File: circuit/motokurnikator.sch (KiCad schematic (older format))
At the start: 13 parts, among them IC1 ATTINY84-P, P1 MOTOR, SW1 END_SW, SW2 END_SW, SW3 MANUAL_OPEN, U1 LM7805CT

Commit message: Add a missing resistor.
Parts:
- added R4: 1k, symbol R
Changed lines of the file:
@@
 L GND #PWR9
 U 1 1 553CC16E
-P 5500 3750
-F 0 "#PWR9" H 5500 3750 30  0001 C CNN
-F 1 "GND" H 5500 3680 30  0001 C CNN
-F 2 "" H 5500 3750 60  0000 C CNN
-F 3 "" H 5500 3750 60  0000 C CNN
-	1    5500 3750
+P 6000 3750
+F 0 "#PWR9" H 6000 3750 30  0001 C CNN
+F 1 "GND" H 6000 3680 30  0001 C CNN
+F 2 "" H 6000 3750 60  0000 C CNN
+F 3 "" H 6000 3750 60  0000 C CNN
+	1    6000 3750
 	0    -1   -1   0
 $EndComp
@@
 Text Notes 10600 7650 0    60   ~ 0
 2
+$Comp
+L R R4
+U 1 1 553D0A76
+P 5750 3750
+F 0 "R4" V 5830 3750 40  0000 C CNN
+F 1 "1k" V 5757 3751 40  0000 C CNN
+F 2 "" V 5680 3750 30  0000 C CNN
+F 3 "" H 5750 3750 30  0000 C CNN
+	1    5750 3750
+	0    1    1    0
+$EndComp
 $EndSCHEMATC

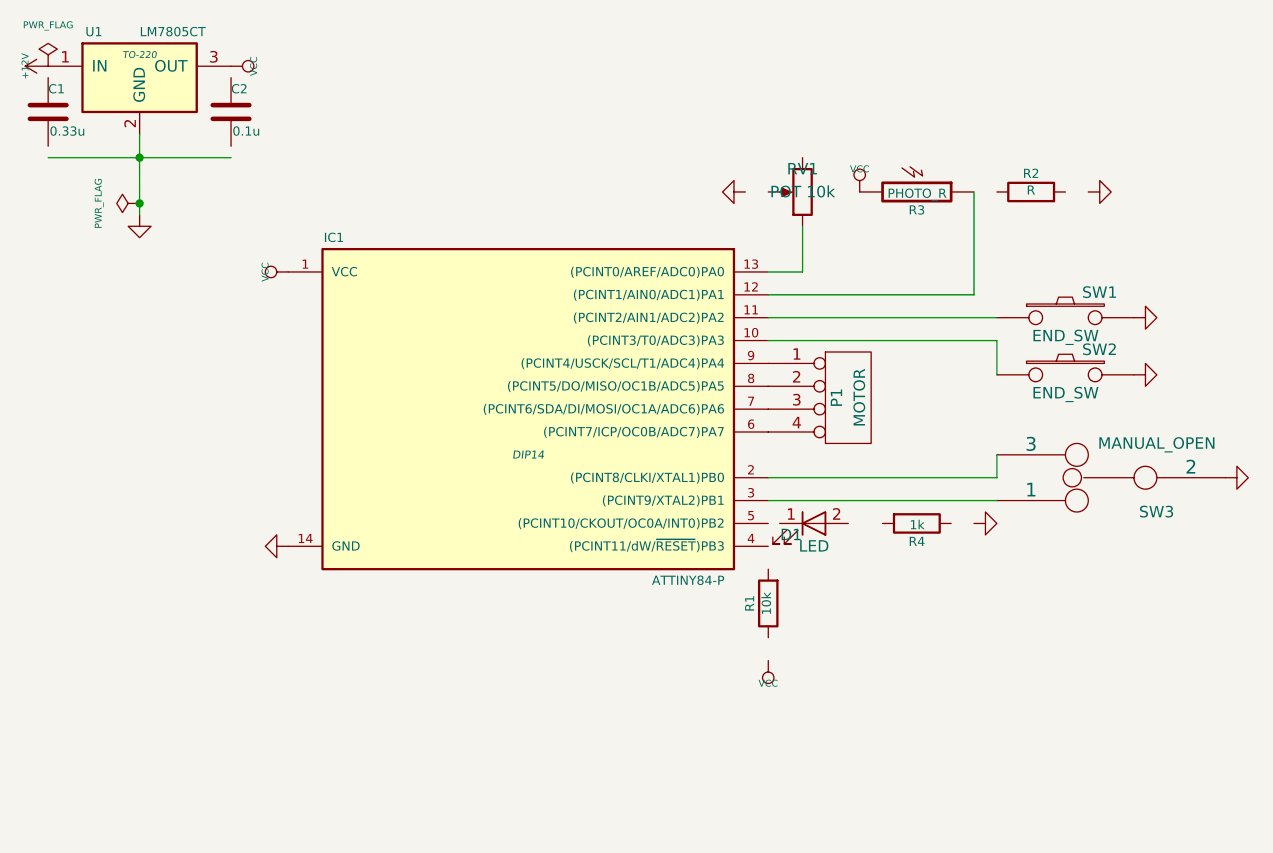
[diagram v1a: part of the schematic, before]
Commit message: Update schematic for newer symbol library.
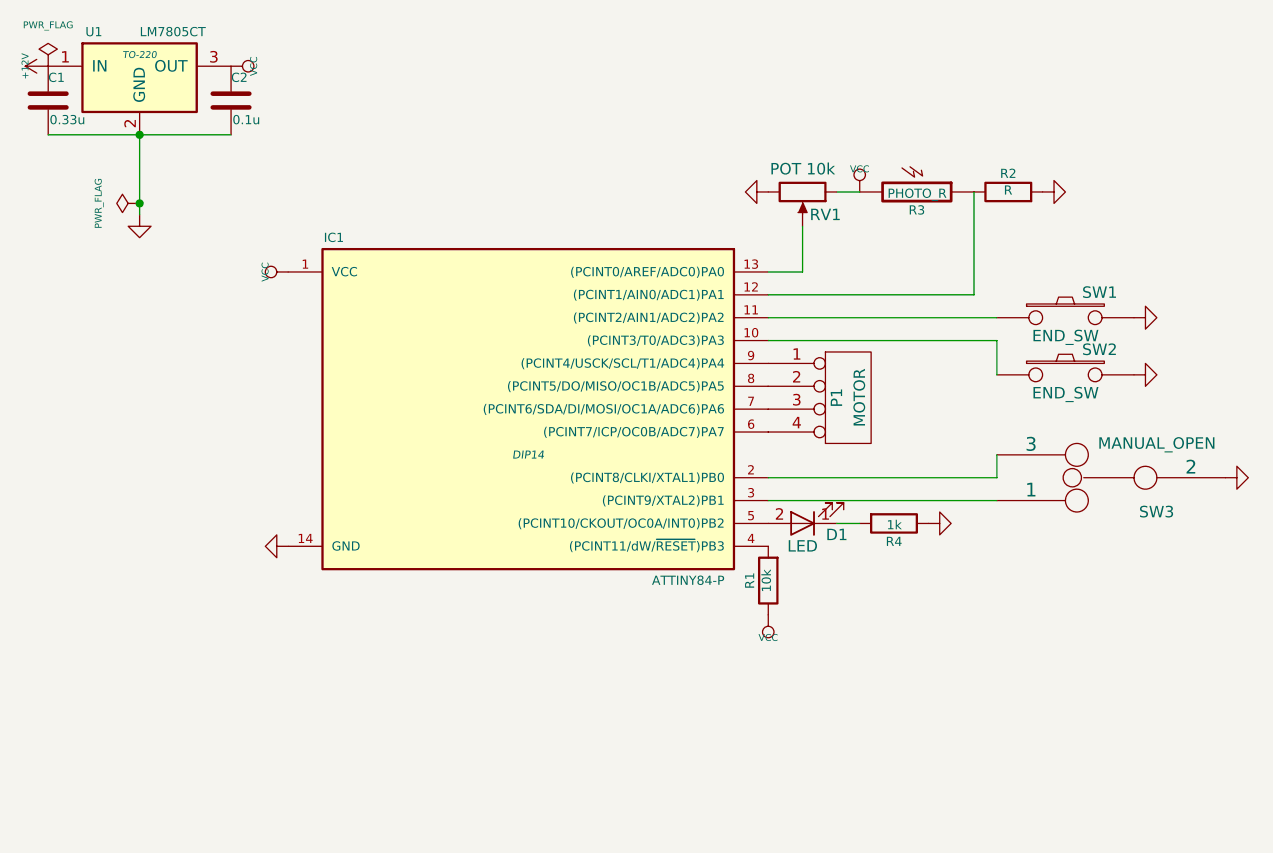
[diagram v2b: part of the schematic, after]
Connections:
- wire segments 12 -> 14
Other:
- moved on the sheet: C1, C2, D1, R1, R2, R4, RV1
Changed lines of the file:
@@
 LIBS:memory
 LIBS:xilinx
-LIBS:special
 LIBS:microcontrollers
 LIBS:dsp
@@
 U 1 1 55212F35
 P 5250 2300
-F 0 "RV1" H 5250 2200 50  0000 C CNN
-F 1 "POT 10k" H 5250 2300 50  0000 C CNN
+F 0 "RV1" V 5350 2400 50  0000 C CNN
+F 1 "POT 10k" V 5150 2300 50  0000 C CNN
 F 2 "" H 5250 2300 60  0000 C CNN
 F 3 "" H 5250 2300 60  0000 C CNN
 	1    5250 2300
-	-1   0    0    1
+	0    1    1    0
 $EndComp
 $Comp
 L GND #PWR6
 U 1 1 55212F76
-P 5000 2300
-F 0 "#PWR6" H 5000 2300 30  0001 C CNN
-F 1 "GND" H 5000 2230 30  0001 C CNN
-F 2 "" H 5000 2300 60  0000 C CNN
-F 3 "" H 5000 2300 60  0000 C CNN
-	1    5000 2300
+P 5100 2300
+F 0 "#PWR6" H 5100 2300 30  0001 C CNN
+F 1 "GND" H 5100 2230 30  0001 C CNN
+F 2 "" H 5100 2300 60  0000 C CNN
+F 3 "" H 5100 2300 60  0000 C CNN
+	1    5100 2300
 	0    1    1    0
 $EndComp
@@
 L R R2
 U 1 1 55212FCB
-P 6250 2300
-F 0 "R2" V 6330 2300 40  0000 C CNN
-F 1 "R" V 6257 2301 40  0000 C CNN
-F 2 "" V 6180 2300 30  0000 C CNN
-F 3 "" H 6250 2300 30  0000 C CNN
-	1    6250 2300
+P 6150 2300
+F 0 "R2" V 6230 2300 40  0000 C CNN
+F 1 "R" V 6157 2301 40  0000 C CNN
+F 2 "" V 6080 2300 30  0000 C CNN
+F 3 "" H 6150 2300 30  0000 C CNN
+	1    6150 2300
 	0    -1   -1   0
 $EndComp
@@
 L GND #PWR10
 U 1 1 55213508
-P 6500 2300
-F 0 "#PWR10" H 6500 2300 30  0001 C CNN
-F 1 "GND" H 6500 2230 30  0001 C CNN
-F 2 "" H 6500 2300 60  0000 C CNN
-F 3 "" H 6500 2300 60  0000 C CNN
-	1    6500 2300
+P 6300 2300
+F 0 "#PWR10" H 6300 2300 30  0001 C CNN
+F 1 "GND" H 6300 2230 30  0001 C CNN
+F 2 "" H 6300 2300 60  0000 C CNN
+F 3 "" H 6300 2300 60  0000 C CNN
+	1    6300 2300
 	0    -1   -1   0
 $EndComp
@@
 L R R1
 U 1 1 5521358D
-P 5100 4100
-F 0 "R1" V 5180 4100 40  0000 C CNN
-F 1 "10k" V 5107 4101 40  0000 C CNN
-F 2 "" V 5030 4100 30  0000 C CNN
-F 3 "" H 5100 4100 30  0000 C CNN
-	1    5100 4100
+P 5100 4000
+F 0 "R1" V 5180 4000 40  0000 C CNN
+F 1 "10k" V 5107 4001 40  0000 C CNN
+F 2 "" V 5030 4000 30  0000 C CNN
+F 3 "" H 5100 4000 30  0000 C CNN
+	1    5100 4000
 	-1   0    0    1
 $EndComp
@@
 L VCC #PWR7
 U 1 1 552135C4
-P 5100 4350
-F 0 "#PWR7" H 5100 4450 30  0001 C CNN
-F 1 "VCC" H 5100 4450 30  0000 C CNN
-F 2 "" H 5100 4350 60  0000 C CNN
-F 3 "" H 5100 4350 60  0000 C CNN
-	1    5100 4350
+P 5100 4150
+F 0 "#PWR7" H 5100 4250 30  0001 C CNN
+F 1 "VCC" H 5100 4250 30  0000 C CNN
+F 2 "" H 5100 4150 60  0000 C CNN
+F 3 "" H 5100 4150 60  0000 C CNN
+	1    5100 4150
 	-1   0    0    1
 $EndComp
@@
 L LED D1
 U 1 1 553CC120
-P 5300 3750
-F 0 "D1" H 5200 3700 50  0000 C CNN
-F 1 "LED" H 5300 3650 50  0000 C CNN
-F 2 "" H 5300 3750 60  0000 C CNN
-F 3 "" H 5300 3750 60  0000 C CNN
-	1    5300 3750
-	1    0    0    -1
+P 5250 3750
+F 0 "D1" H 5100 3800 50  0000 C CNN
+F 1 "LED" H 5250 3850 50  0000 C CNN
+F 2 "" H 5250 3750 60  0000 C CNN
+F 3 "" H 5250 3750 60  0000 C CNN
+	1    5250 3750
+	-1   0    0    1
 $EndComp
 $Comp
 L GND #PWR9
 U 1 1 553CC16E
-P 6000 3750
-F 0 "#PWR9" H 6000 3750 30  0001 C CNN
-F 1 "GND" H 6000 3680 30  0001 C CNN
-F 2 "" H 6000 3750 60  0000 C CNN
-F 3 "" H 6000 3750 60  0000 C CNN
-	1    6000 3750
+P 5800 3750
+F 0 "#PWR9" H 5800 3750 30  0001 C CNN
+F 1 "GND" H 5800 3680 30  0001 C CNN
+F 2 "" H 5800 3750 60  0000 C CNN
+F 3 "" H 5800 3750 60  0000 C CNN
+	1    5800 3750
 	0    -1   -1   0
 $EndComp
@@
 L C C1
 U 1 1 553CC485
-P 1950 1950
-F 0 "C1" H 1950 2050 40  0000 L CNN
-F 1 "0.33u" H 1956 1865 40  0000 L CNN
-F 2 "" H 1988 1800 30  0000 C CNN
-F 3 "" H 1950 1950 60  0000 C CNN
-	1    1950 1950
+P 1950 1900
+F 0 "C1" H 1950 2000 40  0000 L CNN
+F 1 "0.33u" H 1956 1815 40  0000 L CNN
+F 2 "" H 1988 1750 30  0000 C CNN
+F 3 "" H 1950 1900 60  0000 C CNN
+	1    1950 1900
 	1    0    0    -1
 $EndComp
@@
 Connection ~ 2350 2350
 Wire Wire Line
-	1950 2150 2750 2150
-Connection ~ 2350 2150
+	1950 2050 2750 2050
 $Comp
 L C C2
 U 1 1 553CC580
-P 2750 1950
-F 0 "C2" H 2750 2050 40  0000 L CNN
-F 1 "0.1u" H 2756 1865 40  0000 L CNN
-F 2 "" H 2788 1800 30  0000 C CNN
-F 3 "" H 2750 1950 60  0000 C CNN
-	1    2750 1950
+P 2750 1900
+F 0 "C2" H 2750 2000 40  0000 L CNN
+F 1 "0.1u" H 2756 1815 40  0000 L CNN
+F 2 "" H 2788 1750 30  0000 C CNN
+F 3 "" H 2750 1900 60  0000 C CNN
+	1    2750 1900
 	1    0    0    -1
 $EndComp
@@
 L R R4
 U 1 1 553D0A76
-P 5750 3750
-F 0 "R4" V 5830 3750 40  0000 C CNN
-F 1 "1k" V 5757 3751 40  0000 C CNN
-F 2 "" V 5680 3750 30  0000 C CNN
-F 3 "" H 5750 3750 30  0000 C CNN
-	1    5750 3750
-	0    1    1    0
-$EndComp
+P 5650 3750
+F 0 "R4" V 5730 3750 40  0000 C CNN
+F 1 "1k" V 5657 3751 40  0000 C CNN
+F 2 "" V 5580 3750 30  0000 C CNN
+F 3 "" H 5650 3750 30  0000 C CNN
+	1    5650 3750
+	0    1    1    0
+$EndComp
+Connection ~ 2350 2050
+Wire Wire Line
+	5500 2300 5400 2300
+Wire Wire Line
+	5400 3750 5500 3750
 $EndSCHEMATC

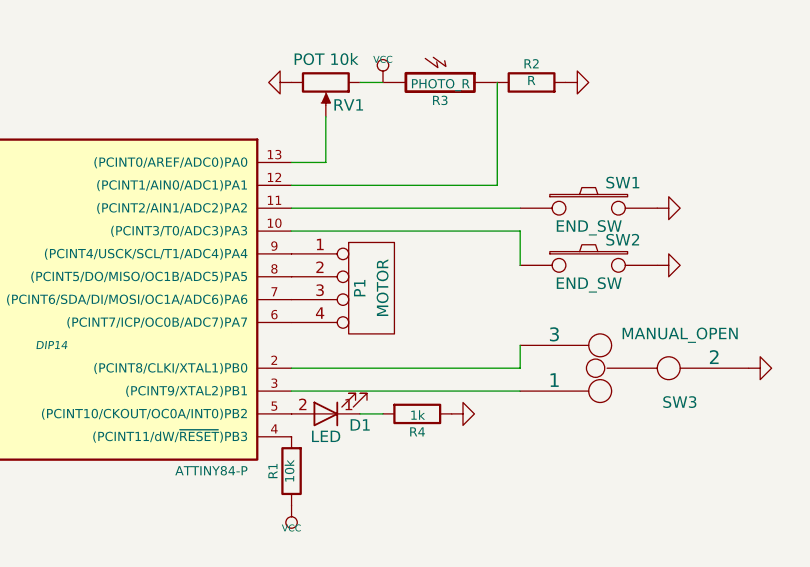
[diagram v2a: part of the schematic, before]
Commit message: Remove support for stepper motors.
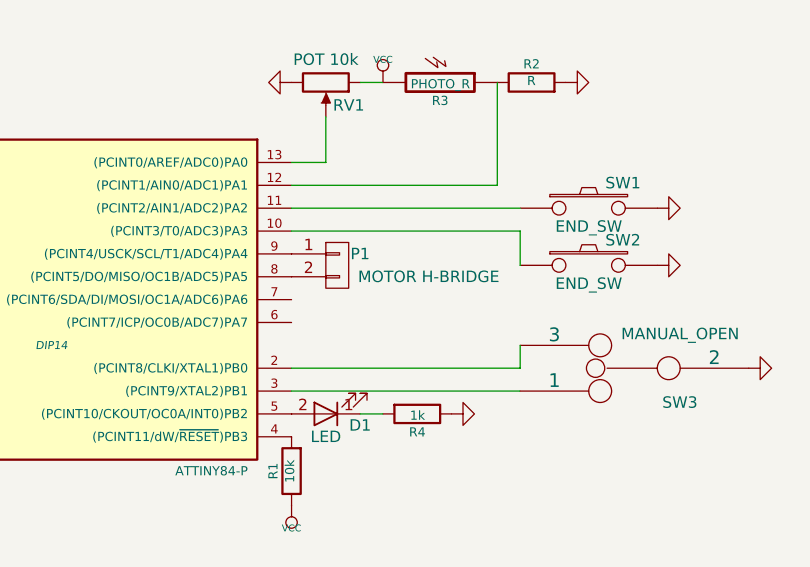
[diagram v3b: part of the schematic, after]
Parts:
- removed P1: MOTOR, symbol CONN_4
- added P1: MOTOR H-BRIDGE, symbol CONN_01X02
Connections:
- net at IC1.8 ((PCINT5/DO/MISO/OC1B/ADC5)PA5): now also P1.2 (P2)
- net at IC1.9 ((PCINT4/USCK/SCL/T1/ADC4)PA4): now also P1.1 (P1)
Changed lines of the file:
@@
-$EndComp
-$Comp
-L CONN_4 P1
-U 1 1 55212E80
-P 5450 3200
-F 0 "P1" V 5400 3200 50  0000 C CNN
-F 1 "MOTOR" V 5500 3200 50  0000 C CNN
-F 2 "" H 5450 3200 60  0000 C CNN
-F 3 "" H 5450 3200 60  0000 C CNN
-	1    5450 3200
-	1    0    0    -1
 $EndComp
 $Comp
@@
 Wire Wire Line
 	5400 3750 5500 3750
+$Comp
+L CONN_01X02 P1
+U 1 1 5A800050
+P 5300 3100
+F 0 "P1" H 5400 3150 50  0000 C CNN
+F 1 "MOTOR H-BRIDGE" H 5700 3050 50  0000 C CNN
+F 2 "" H 5300 3100 50  0001 C CNN
+F 3 "" H 5300 3100 50  0001 C CNN
+	1    5300 3100
+	1    0    0    -1
+$EndComp
 $EndSCHEMATC

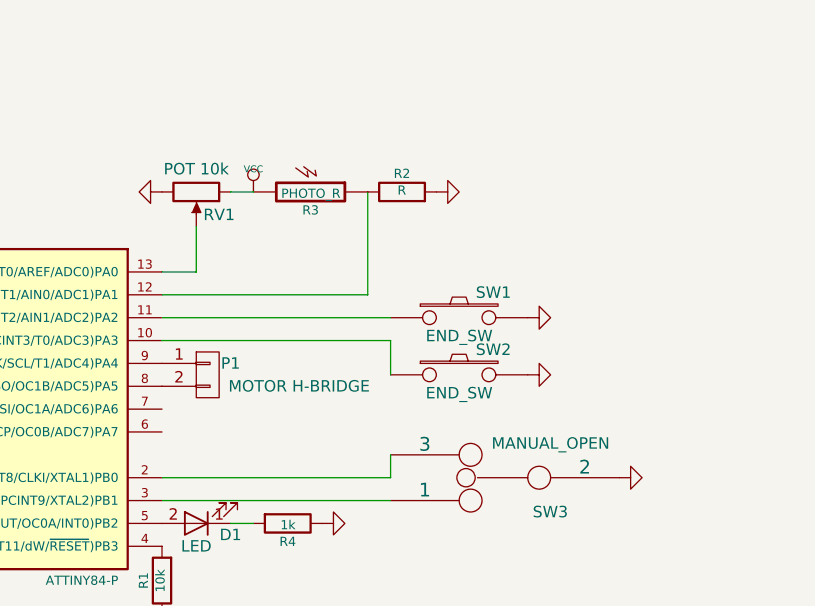
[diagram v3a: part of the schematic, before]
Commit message: Use two pots instead of a fixed hysteresis for easier setting.
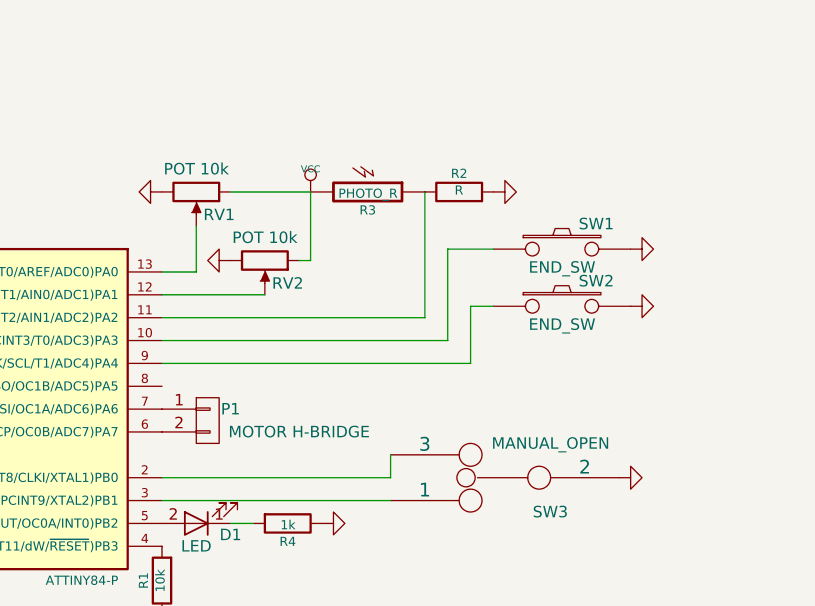
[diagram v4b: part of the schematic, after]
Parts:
- added RV2: POT 10k, symbol POT
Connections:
- net GND: now also RV2.3
- net VCC: now also RV2.1
- net at IC1.10 ((PCINT3/T0/ADC3)PA3): now also SW1.1; no longer SW2.1
- net at IC1.11 ((PCINT2/AIN1/ADC2)PA2): now also R2.1, R3.1; no longer SW1.1
- net at IC1.6 ((PCINT7/ICP/OC0B/ADC7)PA7): now also P1.2 (P2)
- net at IC1.7 ((PCINT6/SDA/DI/MOSI/OC1A/ADC6)PA6): now also P1.1 (P1)
- net at IC1.8 ((PCINT5/DO/MISO/OC1B/ADC5)PA5): no longer P1.2 (P2)
- net at IC1.9 ((PCINT4/USCK/SCL/T1/ADC4)PA4): now also SW2.1; no longer P1.1 (P1)
- new net: IC1.12 ((PCINT1/AIN0/ADC1)PA1), RV2.2
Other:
- moved on the sheet: P1, R2, R3, SW1, SW2
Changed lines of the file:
@@
 L VCC #PWR8
 U 1 1 55212F96
-P 5500 2300
-F 0 "#PWR8" H 5500 2400 30  0001 C CNN
-F 1 "VCC" H 5500 2400 30  0000 C CNN
-F 2 "" H 5500 2300 60  0000 C CNN
-F 3 "" H 5500 2300 60  0000 C CNN
-	1    5500 2300
+P 5750 2300
+F 0 "#PWR8" H 5750 2400 30  0001 C CNN
+F 1 "VCC" H 5750 2400 30  0000 C CNN
+F 2 "" H 5750 2300 60  0000 C CNN
+F 3 "" H 5750 2300 60  0000 C CNN
+	1    5750 2300
 	1    0    0    -1
 $EndComp
@@
 L R R2
 U 1 1 55212FCB
-P 6150 2300
-F 0 "R2" V 6230 2300 40  0000 C CNN
-F 1 "R" V 6157 2301 40  0000 C CNN
-F 2 "" V 6080 2300 30  0000 C CNN
-F 3 "" H 6150 2300 30  0000 C CNN
-	1    6150 2300
+P 6400 2300
+F 0 "R2" V 6480 2300 40  0000 C CNN
+F 1 "R" V 6407 2301 40  0000 C CNN
+F 2 "" V 6330 2300 30  0000 C CNN
+F 3 "" H 6400 2300 30  0000 C CNN
+	1    6400 2300
 	0    -1   -1   0
 $EndComp
@@
 L PHOTO_R R3
 U 1 1 55213320
-P 5750 2300
-F 0 "R3" V 5830 2300 40  0000 C CNN
-F 1 "PHOTO_R" V 5757 2301 40  0000 C CNN
-F 2 "" V 5675 2290 30  0000 C CNN
-F 3 "" H 5750 2300 30  0000 C CNN
-	1    5750 2300
+P 6000 2300
+F 0 "R3" V 6080 2300 40  0000 C CNN
+F 1 "PHOTO_R" V 6007 2301 40  0000 C CNN
+F 2 "" V 5925 2290 30  0000 C CNN
+F 3 "" H 6000 2300 30  0000 C CNN
+	1    6000 2300
 	0    1    1    0
 $EndComp
@@
 L GND #PWR10
 U 1 1 55213508
-P 6300 2300
-F 0 "#PWR10" H 6300 2300 30  0001 C CNN
-F 1 "GND" H 6300 2230 30  0001 C CNN
-F 2 "" H 6300 2300 60  0000 C CNN
-F 3 "" H 6300 2300 60  0000 C CNN
-	1    6300 2300
-	0    -1   -1   0
-$EndComp
-Wire Wire Line
-	5100 2750 6000 2750
-Wire Wire Line
-	6000 2750 6000 2300
+P 6550 2300
+F 0 "#PWR10" H 6550 2300 30  0001 C CNN
+F 1 "GND" H 6550 2230 30  0001 C CNN
+F 2 "" H 6550 2300 60  0000 C CNN
+F 3 "" H 6550 2300 60  0000 C CNN
+	1    6550 2300
+	0    -1   -1   0
+$EndComp
+Wire Wire Line
+	6250 2850 5100 2850
+Wire Wire Line
+	6250 2300 6250 2850
 $Comp
 L R R1
@@
 L SW_PUSH SW1
 U 1 1 552135D8
-P 6400 2850
-F 0 "SW1" H 6550 2960 50  0000 C CNN
-F 1 "END_SW" H 6400 2770 50  0000 C CNN
-F 2 "" H 6400 2850 60  0000 C CNN
-F 3 "" H 6400 2850 60  0000 C CNN
-	1    6400 2850
+P 6850 2550
+F 0 "SW1" H 7000 2660 50  0000 C CNN
+F 1 "END_SW" H 6850 2470 50  0000 C CNN
+F 2 "" H 6850 2550 60  0000 C CNN
+F 3 "" H 6850 2550 60  0000 C CNN
+	1    6850 2550
 	1    0    0    -1
 $EndComp
@@
 L SW_PUSH SW2
 U 1 1 5521361E
-P 6400 3100
-F 0 "SW2" H 6550 3210 50  0000 C CNN
-F 1 "END_SW" H 6400 3020 50  0000 C CNN
-F 2 "" H 6400 3100 60  0000 C CNN
-F 3 "" H 6400 3100 60  0000 C CNN
-	1    6400 3100
-	1    0    0    -1
-$EndComp
-Wire Wire Line
-	5100 2850 6100 2850
-Wire Wire Line
-	5100 2950 6100 2950
-Wire Wire Line
-	6100 2950 6100 3100
+P 6850 2800
+F 0 "SW2" H 7000 2910 50  0000 C CNN
+F 1 "END_SW" H 6850 2720 50  0000 C CNN
+F 2 "" H 6850 2800 60  0000 C CNN
+F 3 "" H 6850 2800 60  0000 C CNN
+	1    6850 2800
+	1    0    0    -1
+$EndComp
+Wire Wire Line
+	5100 2950 6350 2950
+Wire Wire Line
+	5100 3050 6450 3050
 $Comp
 L GND #PWR11
 U 1 1 552136A3
-P 6700 2850
-F 0 "#PWR11" H 6700 2850 30  0001 C CNN
-F 1 "GND" H 6700 2780 30  0001 C CNN
-F 2 "" H 6700 2850 60  0000 C CNN
-F 3 "" H 6700 2850 60  0000 C CNN
-	1    6700 2850
+P 7150 2550
+F 0 "#PWR11" H 7150 2550 30  0001 C CNN
+F 1 "GND" H 7150 2480 30  0001 C CNN
+F 2 "" H 7150 2550 60  0000 C CNN
+F 3 "" H 7150 2550 60  0000 C CNN
+	1    7150 2550
 	0    -1   -1   0
 $EndComp
@@
 L GND #PWR12
 U 1 1 552136B7
-P 6700 3100
-F 0 "#PWR12" H 6700 3100 30  0001 C CNN
-F 1 "GND" H 6700 3030 30  0001 C CNN
-F 2 "" H 6700 3100 60  0000 C CNN
-F 3 "" H 6700 3100 60  0000 C CNN
-	1    6700 3100
+P 7150 2800
+F 0 "#PWR12" H 7150 2800 30  0001 C CNN
+F 1 "GND" H 7150 2730 30  0001 C CNN
+F 2 "" H 7150 2800 60  0000 C CNN
+F 3 "" H 7150 2800 60  0000 C CNN
+	1    7150 2800
 	0    -1   -1   0
 $EndComp
@@
 Connection ~ 2350 2050
 Wire Wire Line
-	5500 2300 5400 2300
+	5400 2300 5750 2300
 Wire Wire Line
 	5400 3750 5500 3750
@@
 L CONN_01X02 P1
 U 1 1 5A800050
-P 5300 3100
-F 0 "P1" H 5400 3150 50  0000 C CNN
-F 1 "MOTOR H-BRIDGE" H 5700 3050 50  0000 C CNN
-F 2 "" H 5300 3100 50  0001 C CNN
-F 3 "" H 5300 3100 50  0001 C CNN
-	1    5300 3100
-	1    0    0    -1
-$EndComp
+P 5300 3300
+F 0 "P1" H 5400 3350 50  0000 C CNN
+F 1 "MOTOR H-BRIDGE" H 5700 3250 50  0000 C CNN
+F 2 "" H 5300 3300 50  0001 C CNN
+F 3 "" H 5300 3300 50  0001 C CNN
+	1    5300 3300
+	1    0    0    -1
+$EndComp
+$Comp
+L POT RV2
+U 1 1 5A8007FB
+P 5550 2600
+F 0 "RV2" V 5650 2700 50  0000 C CNN
+F 1 "POT 10k" V 5450 2600 50  0000 C CNN
+F 2 "" H 5550 2600 60  0000 C CNN
+F 3 "" H 5550 2600 60  0000 C CNN
+	1    5550 2600
+	0    1    1    0
+$EndComp
+$Comp
+L GND #PWR?
+U 1 1 5A800C64
+P 5400 2600
+F 0 "#PWR?" H 5400 2600 30  0001 C CNN
+F 1 "GND" H 5400 2530 30  0001 C CNN
+F 2 "" H 5400 2600 60  0000 C CNN
+F 3 "" H 5400 2600 60  0000 C CNN
+	1    5400 2600
+	0    1    1    0
+$EndComp
+Wire Wire Line
+	5550 2750 5100 2750
+Wire Wire Line
+	5750 2300 5750 2600
+Wire Wire Line
+	5750 2600 5700 2600
+Wire Wire Line
+	6350 2950 6350 2550
+Wire Wire Line
+	6350 2550 6550 2550
+Wire Wire Line
+	6450 3050 6450 2800
+Wire Wire Line
+	6450 2800 6550 2800
 $EndSCHEMATC
